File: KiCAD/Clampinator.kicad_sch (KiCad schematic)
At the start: 113 parts, among them J2 Conn_01x02_Socket, J20 VP0265840000G, J21 Conn_01x03_Socket, J22 Conn_01x03_Socket, J23 VP0265840000G, J24 VP0265840000G, J25 +5V INJ, J3 Conn_01x02_Socket, J4 Conn_01x02_Socket, Q1 TK100E10N1,S1X, Q2 TK100E10N1,S1X, Q3 TK100E10N1,S1X, Q4 TK100E10N1,S1X, Q5 TK100E10N1,S1X, Q9 MMBT3904-C20526, SW6 EG1847-ND, SW7 GPI-154-3013, U10 LM74810QDRRRQ1, U14 LM5163DDAR, U2 TL432BQDBZR, U3 EG2131, U4 UCC33420RAQR_C46461551, U6 LM5012DDAR, U9 EL357N

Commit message: Sync KiCAD project
Forgot to push this earlier
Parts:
- C1, C2: LCSC Part (none) -> C178408
- C3, C44, C47, C48, C58, C59: LCSC Part (none) -> C915836
- C33, C35: LCSC Part (none) -> C1548
- C34: LCSC Part (none) -> C15850
- C36: LCSC Part (none) -> C12891
- C39, C49, C52, C53, C54, C55: LCSC Part (none) -> C5122251
- C4: LCSC Part (none) -> C307331
- C40, C50: LCSC Part (none) -> C1604
- C41, C45, C46: LCSC Part (none) -> C542593
- C42, C51: LCSC Part (none) -> C1546
- C43, C56: LCSC Part (none) -> C12891; now in the parts list
- C57: LCSC Part (none) -> C393168
- C7, R50: now left out of the parts list
- D11: LCSC Part (none) -> C65010
- D4, D7, D8: LCSC Part (none) -> C8678
- L1: LCSC Part (none) -> C7431083
- L2: LCSC Part (none) -> C6069597
- L3: LCSC Part (none) -> C2041395
- R1, R6, R7, R8, R9: LCSC Part (none) -> C17415
- R10: LCSC Part (none) -> C25752
- R11: LCSC Part (none) -> C25900
- R12: LCSC Part (none) -> C17902
- R13, R45: LCSC Part (none) -> C17900
- R2: LCSC Part (none) -> C2849357
- R29: LCSC Part (none) -> C23228
- R3: LCSC Part (none) -> C23179
- R32, R51: LCSC Part (none) -> C25744
- R37: LCSC Part (none) -> C17414
- R39, R53: LCSC Part (none) -> C25808
- R4: LCSC Part (none) -> C23192
- R40: LCSC Part (none) -> C24436
- R41: LCSC Part (none) -> C245981
- R42: LCSC Part (none) -> C23184
- R43: LCSC Part (none) -> C79297
- R44: LCSC Part (none) -> C4184
- R46: LCSC Part (none) -> C2077219
- R47: LCSC Part (none) -> C185340
- R48: LCSC Part (none) -> C7302896
- R49: LCSC Part (none) -> C25334
- R5: LCSC Part (none) -> C17709
- RV1: LCSC Part (none) -> C49190460
- U2: LCSC Part (none) -> C53724

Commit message: Oscillator Test Pads + Re-Fix USB-C
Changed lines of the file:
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@@
 	)
 	(junction
+		(at 264.16 158.75)
+		(diameter 0)
+		(color 0 0 0 0)
+	)
+	(junction
 		(at 128.27 175.26)
 		(diameter 0)
@@
 	(wire
 		(pts
+			(xy 264.16 158.75) (xy 264.16 160.02)
+		)
+		(stroke
+			(width 0)
+			(type default)
+		)
+	)
+	(wire
+		(pts
 			(xy 39.37 92.71) (xy 39.37 91.44)
 		)
@@
 		(length 2.54)
 		(shape round)
-		(at 264.16 158.75 180)
+		(at 264.16 160.02 180)
 		(fields_autoplaced yes)
 		(effects
@@
 		)
 		(property "Netclass" "Default"
-			(at 264.8585 161.29 0)
+			(at 264.8585 162.56 0)
 			(show_name no)
 			(do_not_autoplace no)
@@
 		)
 		(property "Component Class" ""
-			(at 41.91 101.6 0)
+			(at 41.91 102.87 0)
 			(show_name no)
 			(do_not_autoplace no)

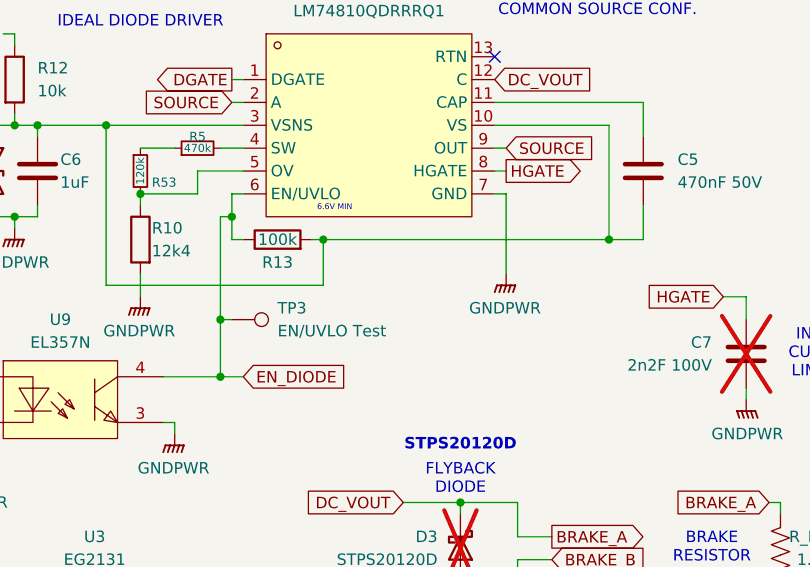
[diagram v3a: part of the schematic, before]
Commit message: Shrunk edge cuts, Started fixing GND fills, Changed pad shapes, Nudged footprints around
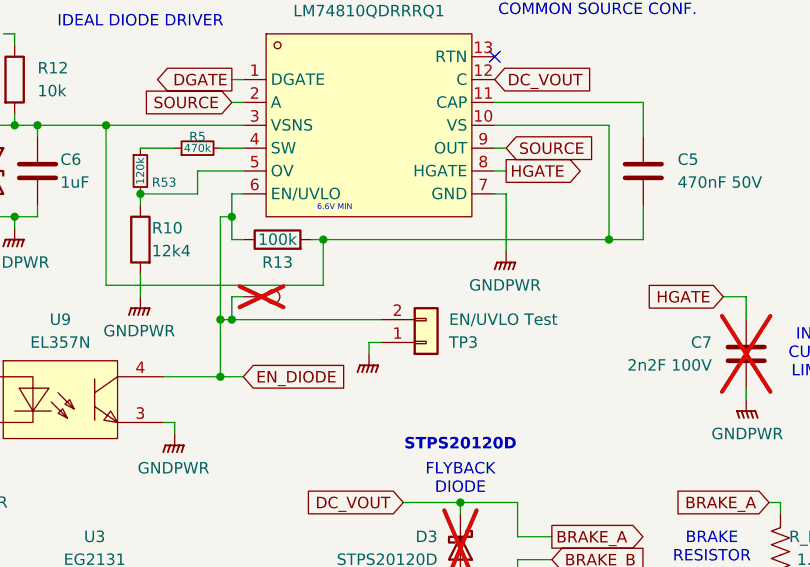
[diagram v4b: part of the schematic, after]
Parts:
- added TP3: EN/UVLO Test, Connector_PinHeader_2.54mm:PinHeader_1x02_P2.54mm_Vertical, symbol Connector_Generic:Conn_01x02
- TP-not3: renamed from TP3; now not fitted
- TP2: footprint TestPoint:TestPoint_THTPad_D2.0mm_Drill1.0mm -> Connector_PinHeader_2.54mm:PinHeader_1x01_P2.54mm_Vertical
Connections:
- net EN_DIODE: now also TP3.2 (Pin_2)
- net GNDPWR: now also TP3.1 (Pin_1)

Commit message: Change some TPs to 2.54mm pin headers, silkscreen changes, start led redo
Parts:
- TP11: footprint TestPoint:TestPoint_THTPad_D1.5mm_Drill0.7mm -> Connector_PinHeader_2.54mm:PinHeader_1x01_P2.54mm_Vertical
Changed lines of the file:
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@@
 			)
 		)
-		(property "Footprint" "TestPoint:TestPoint_THTPad_D1.5mm_Drill0.7mm"
+		(property "Footprint" "Connector_PinHeader_2.54mm:PinHeader_1x01_P2.54mm_Vertical"
 			(at 203.2 144.78 0)
 			(hide yes)

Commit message: Swap out input TVS for 14S maximum, relinked easyeda2kicad library, added extra shunting NMOS (DNP-ed)
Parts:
- added Q6: TK100E10N1,S1X, easyeda2kicad:TO-220-3_L10.0-W4.5-P2.54-L, symbol Simulation_SPICE:NMOS
- added TP13: TestPoint, TestPoint:TestPoint_THTPad_D1.5mm_Drill0.7mm, symbol Connector:TestPoint
- added TP14: D, TestPoint:TestPoint_THTPad_D1.0mm_Drill0.5mm, symbol Connector:TestPoint
- added TP15: H, TestPoint:TestPoint_THTPad_D1.0mm_Drill0.5mm, symbol Connector:TestPoint
- D1: value SMCJ60CA -> SMCJ54CA; LCSC Part C135187 -> C135179; LPN C135187 -> C135179; MPN SMCJ60CA-13-F -> SMCJ54CA-13-F
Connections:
- net BRAKE_B: now also Q6.1 (D)
- net DGATE: now also TP14.1
- net GNDPWR: now also Q6.3 (S)
- net HGATE: now also TP15.1
- net at Q5.2 (G), R1.1, R37.1: now also Q6.2 (G)
- net at R10.1, R53.2, U10.5 (OV): now also TP13.1

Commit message: Fixed footprint libraries, corrected terminal block footprints, added 3d model for precharge resistor terminal block
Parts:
- added TP16: PGND, TestPoint:TestPoint_THTPad_D2.0mm_Drill1.0mm, symbol Connector:TestPoint
- J20, J24: value VP0265840000G -> VP0365840000G
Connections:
- net GNDPWR: now also TP16.1
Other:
- note removed: "(PRECHARGE RESISTOR)"
- note removed: "NEED TO FIX FOOTPRINT FOR ALL 8 PADS"
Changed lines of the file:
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@@
 		)
 	)
-	(text "NEED TO FIX FOOTPRINT FOR ALL 8 PADS"
-		(exclude_from_sim no)
-		(at 266.7 247.65 0)
-		(effects
-			(font
-				(size 1.27 1.27)
-				(thickness 0.254)
-				(bold yes)
-				(color 255 0 0 1)
-			)
-		)
-	)
 	(text "11 to +20V"
 		(exclude_from_sim no)
@@
 		)
 	)
-	(text "(PRECHARGE\nRESISTOR)"
-		(exclude_from_sim no)
-		(at 320.04 259.08 0)
-		(effects
-			(font
-				(size 1.27 1.27)
-				(thickness 0.254)
-				(bold yes)
-				(color 255 0 0 1)
-			)
-		)
-	)
 	(text "BRAKE\nRESISTOR"
 		(exclude_from_sim no)
@@
 	(wire
 		(pts
+			(xy 57.15 179.07) (xy 57.15 185.42)
+		)
+		(stroke
+			(width 0)
+			(type default)
+		)
+	)
+	(wire
+		(pts
 			(xy 243.84 26.67) (xy 247.65 26.67)
 		)
@@
 	)
 	(symbol
+		(lib_id "Connector:TestPoint")
+		(at 57.15 179.07 0)
+		(mirror y)
+		(unit 1)
+		(body_style 1)
+		(exclude_from_sim no)
+		(in_bom no)
+		(on_board yes)
+		(in_pos_files yes)
+		(dnp no)
+		(property "Reference" "TP16"
+			(at 59.69 177.0381 0)
+			(show_name no)
+			(do_not_autoplace no)
+			(effects
+				(font
+					(size 1.27 1.27)
+				)
+				(justify right)
+			)
+		)
+		(property "Value" "PGND"
+			(at 59.69 174.4981 0)
+			(show_name no)
+			(do_not_autoplace no)
+			(effects
+				(font
+					(size 1.27 1.27)
+				)
+				(justify right)
+			)
+		)
+		(property "Footprint" "TestPoint:TestPoint_THTPad_D2.0mm_Drill1.0mm"
+			(at 52.07 179.07 0)
+			(hide yes)
+			(show_name no)
+			(do_not_autoplace no)
+			(effects
+				(font
+					(size 1.27 1.27)
+				)
+			)
+		)
+		(property "Datasheet" ""
+			(at 52.07 179.07 0)
+			(hide yes)
+			(show_name no)
+			(do_not_autoplace no)
+			(effects
+				(font
+					(size 1.27 1.27)
+				)
+			)
+		)
+		(property "Description" "test point"
+			(at 57.15 179.07 0)
+			(hide yes)
+			(show_name no)
+			(do_not_autoplace no)
+			(effects
+				(font
+					(size 1.27 1.27)
+				)
+			)
+		)
+		(property "DigiKey BOM" ""
+			(at 57.15 179.07 0)
+			(hide yes)
+			(show_name no)
+			(do_not_autoplace no)
+			(effects
+				(font
+					(size 1.27 1.27)
+				)
+			)
+		)
+		(pin "1"
+		)
+		(instances
+			(project "Clampinator"
+				(path "/2e882f49-6d2d-4454-9c69-d6f4a7d50c65"
+					(reference "TP16")
+					(unit 1)
+				)
+			)
+		)
+	)
+	(symbol
 		(lib_id "Device:R_Small")
 		(at 207.01 83.82 90)
@@
 			)
 		)
-		(property "Value" "VP0265840000G"
+		(property "Value" "VP0365840000G"
 			(at 222.25 179.0699 0)
 			(show_name no)
@@
 			)
 		)
-		(property "Datasheet" "VP0265840000G"
+		(property "Datasheet" "https://www.anytek.com.tw/UserUpFiles/20181025/d41_CP3hmn_a.pdf"
 			(at 208.534 163.83 0)
 			(hide yes)
@@
 	)
 	(symbol
+		(lib_id "power:GNDPWR")
+		(at 57.15 185.42 0)
+		(unit 1)
+		(body_style 1)
+		(exclude_from_sim no)
+		(in_bom yes)
+		(on_board yes)
+		(in_pos_files yes)
+		(dnp no)
+		(fields_autoplaced yes)
+		(property "Reference" "#PWR0127"
+			(at 57.15 190.5 0)
+			(hide yes)
+			(show_name no)
+			(do_not_autoplace no)
+			(effects
+				(font
+					(size 1.27 1.27)
+				)
+			)
+		)
+		(property "Value" "GNDPWR"
+			(at 57.023 189.23 0)
+			(show_name no)
+			(do_not_autoplace no)
+			(effects
+				(font
+					(size 1.27 1.27)
+				)
+			)
+		)
+		(property "Footprint" ""
+			(at 57.15 186.69 0)
+			(hide yes)
+			(show_name no)
+			(do_not_autoplace no)
+			(effects
+				(font
+					(size 1.27 1.27)
+				)
+			)
+		)
+		(property "Datasheet" ""
+			(at 57.15 186.69 0)
+			(hide yes)
+			(show_name no)
+			(do_not_autoplace no)
+			(effects
+				(font
+					(size 1.27 1.27)
+				)
+			)
+		)
+		(property "Description" "Power symbol creates a global label with name \"GNDPWR\" , global ground"
+			(at 57.15 185.42 0)
+			(hide yes)
+			(show_name no)
+			(do_not_autoplace no)
+			(effects
+				(font
+					(size 1.27 1.27)
+				)
+			)
+		)
+		(pin "1"
+		)
+		(instances
+			(project "Clampinator"
+				(path "/2e882f49-6d2d-4454-9c69-d6f4a7d50c65"
+					(reference "#PWR0127")
+					(unit 1)
+				)
+			)
+		)
+	)
+	(symbol
 		(lib_id "Device:R_US")
 		(at 200.66 54.61 90)
@@
 			)
 		)
-		(property "Value" "VP0265840000G"
+		(property "Value" "VP0365840000G"
 			(at 222.25 171.4499 0)
 			(show_name no)
@@
 			)
 		)
-		(property "Datasheet" "VP0265840000G"
+		(property "Datasheet" "https://www.anytek.com.tw/UserUpFiles/20181025/d41_CP3hmn_a.pdf"
 			(at 208.534 156.21 0)
 			(hide yes)
